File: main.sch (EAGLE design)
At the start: 67 parts, among them IC10 FGPMMOPA6H, IC2 25LC1024-I/P, IC6 MPL3115A2LGA, IC7 FXAS21000, IC8 ADXL343BCCZ, Q1 12MHz, Q2 MCP9700A-E/TO, Q3 FQP7P06, U1 ATMEGA1284P-PU, U2 LT3570EFEPBF, U3 TL431BQLP

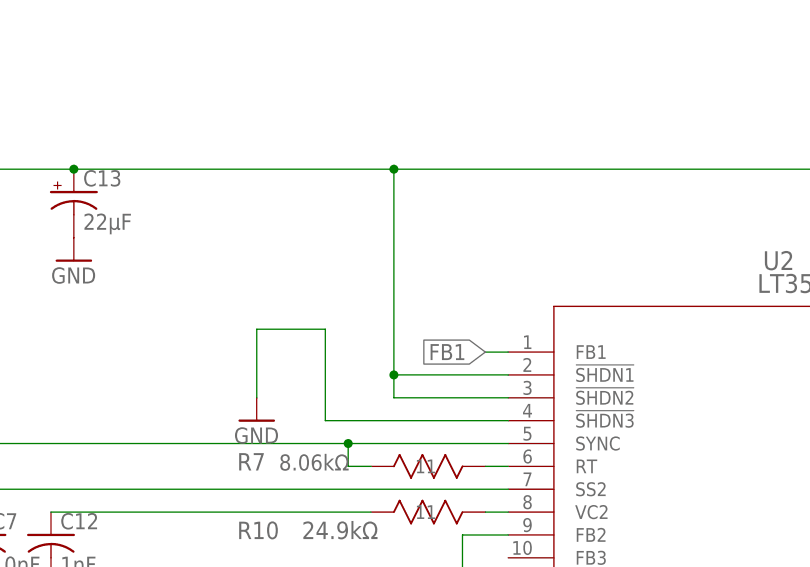
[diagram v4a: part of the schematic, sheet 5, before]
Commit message: Updated Datasheets
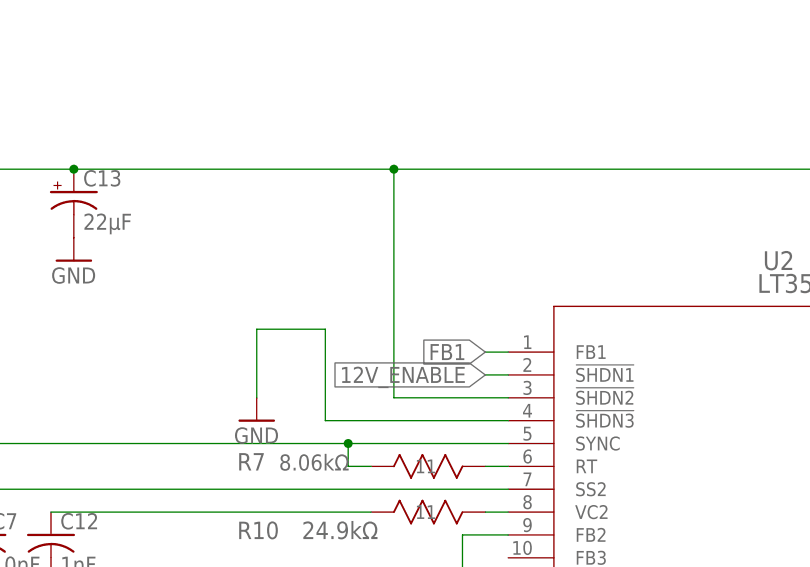
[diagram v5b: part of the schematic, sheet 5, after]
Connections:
- new net 12V_ENABLE: U2.!SHDN1
- net PWR_JUNC: no longer U2.!SHDN1
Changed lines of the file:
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@@
 <grid distance="0.1" unitdist="inch" unit="inch" style="lines" multiple="1" display="no" altdistance="0.01" altunitdist="inch" altunit="inch"/>
 <layers>
-<layer number="1" name="Top" color="4" fill="1" visible="yes" active="no"/>
-<layer number="2" name="Route2" color="1" fill="3" visible="yes" active="no"/>
-<layer number="3" name="Route3" color="4" fill="3" visible="yes" active="no"/>
-<layer number="4" name="Route4" color="1" fill="4" visible="yes" active="no"/>
-<layer number="5" name="Route5" color="4" fill="4" visible="yes" active="no"/>
-<layer number="6" name="Route6" color="1" fill="8" visible="yes" active="no"/>
-<layer number="7" name="Route7" color="4" fill="8" visible="yes" active="no"/>
-<layer number="8" name="Route8" color="1" fill="2" visible="yes" active="no"/>
-<layer number="9" name="Route9" color="4" fill="2" visible="yes" active="no"/>
-<layer number="10" name="Route10" color="1" fill="7" visible="yes" active="no"/>
-<layer number="11" name="Route11" color="4" fill="7" visible="yes" active="no"/>
-<layer number="12" name="Route12" color="1" fill="5" visible="yes" active="no"/>
-<layer number="13" name="Route13" color="4" fill="5" visible="yes" active="no"/>
-<layer number="14" name="Route14" color="1" fill="6" visible="yes" active="no"/>
-<layer number="15" name="Route15" color="4" fill="6" visible="yes" active="no"/>
-<layer number="16" name="Bottom" color="1" fill="1" visible="yes" active="no"/>
-<layer number="17" name="Pads" color="2" fill="1" visible="yes" active="no"/>
-<layer number="18" name="Vias" color="2" fill="1" visible="yes" active="no"/>
-<layer number="19" name="Unrouted" color="6" fill="1" visible="yes" active="no"/>
-<layer number="20" name="Dimension" color="24" fill="1" visible="yes" active="no"/>
-<layer number="21" name="tPlace" color="7" fill="1" visible="yes" active="no"/>
-<layer number="22" name="bPlace" color="7" fill="1" visible="yes" active="no"/>
-<layer number="23" name="tOrigins" color="15" fill="1" visible="yes" active="no"/>
-<layer number="24" name="bOrigins" color="15" fill="1" visible="yes" active="no"/>
-<layer number="25" name="tNames" color="7" fill="1" visible="yes" active="no"/>
-<layer number="26" name="bNames" color="7" fill="1" visible="yes" active="no"/>
-<layer number="27" name="tValues" color="7" fill="1" visible="yes" active="no"/>
-<layer number="28" name="bValues" color="7" fill="1" visible="yes" active="no"/>
+<layer number="1" name="Top" color="4" fill="1" visible="no" active="no"/>
+<layer number="2" name="Route2" color="1" fill="3" visible="no" active="no"/>
+<layer number="3" name="Route3" color="4" fill="3" visible="no" active="no"/>
+<layer number="4" name="Route4" color="1" fill="4" visible="no" active="no"/>
+<layer number="5" name="Route5" color="4" fill="4" visible="no" active="no"/>
+<layer number="6" name="Route6" color="1" fill="8" visible="no" active="no"/>
+<layer number="7" name="Route7" color="4" fill="8" visible="no" active="no"/>
+<layer number="8" name="Route8" color="1" fill="2" visible="no" active="no"/>
+<layer number="9" name="Route9" color="4" fill="2" visible="no" active="no"/>
+<layer number="10" name="Route10" color="1" fill="7" visible="no" active="no"/>
+<layer number="11" name="Route11" color="4" fill="7" visible="no" active="no"/>
+<layer number="12" name="Route12" color="1" fill="5" visible="no" active="no"/>
+<layer number="13" name="Route13" color="4" fill="5" visible="no" active="no"/>
+<layer number="14" name="Route14" color="1" fill="6" visible="no" active="no"/>
+<layer number="15" name="Route15" color="4" fill="6" visible="no" active="no"/>
+<layer number="16" name="Bottom" color="1" fill="1" visible="no" active="no"/>
+<layer number="17" name="Pads" color="2" fill="1" visible="no" active="no"/>
+<layer number="18" name="Vias" color="2" fill="1" visible="no" active="no"/>
+<layer number="19" name="Unrouted" color="6" fill="1" visible="no" active="no"/>
+<layer number="20" name="Dimension" color="24" fill="1" visible="no" active="no"/>
+<layer number="21" name="tPlace" color="7" fill="1" visible="no" active="no"/>
+<layer number="22" name="bPlace" color="7" fill="1" visible="no" active="no"/>
+<layer number="23" name="tOrigins" color="15" fill="1" visible="no" active="no"/>
+<layer number="24" name="bOrigins" color="15" fill="1" visible="no" active="no"/>
+<layer number="25" name="tNames" color="7" fill="1" visible="no" active="no"/>
+<layer number="26" name="bNames" color="7" fill="1" visible="no" active="no"/>
+<layer number="27" name="tValues" color="7" fill="1" visible="no" active="no"/>
+<layer number="28" name="bValues" color="7" fill="1" visible="no" active="no"/>
 <layer number="29" name="tStop" color="7" fill="3" visible="no" active="no"/>
 <layer number="30" name="bStop" color="7" fill="6" visible="no" active="no"/>
@@
 <layer number="35" name="tGlue" color="7" fill="4" visible="no" active="no"/>
 <layer number="36" name="bGlue" color="7" fill="5" visible="no" active="no"/>
-<layer number="37" name="tTest" color="7" fill="1" visible="yes" active="no"/>
-<layer number="38" name="bTest" color="7" fill="1" visible="yes" active="no"/>
+<layer number="37" name="tTest" color="7" fill="1" visible="no" active="no"/>
+<layer number="38" name="bTest" color="7" fill="1" visible="no" active="no"/>
 <layer number="39" name="tKeepout" color="4" fill="11" visible="no" active="no"/>
 <layer number="40" name="bKeepout" color="1" fill="11" visible="no" active="no"/>
@@
 <layer number="44" name="Drills" color="7" fill="1" visible="no" active="no"/>
 <layer number="45" name="Holes" color="7" fill="1" visible="no" active="no"/>
-<layer number="46" name="Milling" color="3" fill="1" visible="yes" active="no"/>
-<layer number="47" name="Measures" color="7" fill="1" visible="yes" active="no"/>
-<layer number="48" name="Document" color="7" fill="1" visible="yes" active="no"/>
-<layer number="49" name="Reference" color="7" fill="1" visible="yes" active="no"/>
-<layer number="50" name="dxf" color="7" fill="1" visible="yes" active="no"/>
-<layer number="51" name="tDocu" color="7" fill="1" visible="yes" active="no"/>
-<layer number="52" name="bDocu" color="7" fill="1" visible="yes" active="no"/>
-<layer number="53" name="tGND_GNDA" color="7" fill="9" visible="yes" active="no"/>
-<layer number="54" name="bGND_GNDA" color="1" fill="9" visible="yes" active="no"/>
-<layer number="56" name="wert" color="7" fill="1" visible="yes" active="no"/>
-<layer number="57" name="tCAD" color="7" fill="1" visible="yes" active="no"/>
-<layer number="59" name="tCarbon" color="7" fill="1" visible="yes" active="no"/>
-<layer number="60" name="bCarbon" color="7" fill="1" visible="yes" active="no"/>
+<layer number="46" name="Milling" color="3" fill="1" visible="no" active="no"/>
+<layer number="47" name="Measures" color="7" fill="1" visible="no" active="no"/>
+<layer number="48" name="Document" color="7" fill="1" visible="no" active="no"/>
+<layer number="49" name="Reference" color="7" fill="1" visible="no" active="no"/>
+<layer number="50" name="dxf" color="7" fill="1" visible="no" active="no"/>
+<layer number="51" name="tDocu" color="7" fill="1" visible="no" active="no"/>
+<layer number="52" name="bDocu" color="7" fill="1" visible="no" active="no"/>
+<layer number="53" name="tGND_GNDA" color="7" fill="9" visible="no" active="no"/>
+<layer number="54" name="bGND_GNDA" color="1" fill="9" visible="no" active="no"/>
+<layer number="56" name="wert" color="7" fill="1" visible="no" active="no"/>
+<layer number="57" name="tCAD" color="7" fill="1" visible="no" active="no"/>
+<layer number="59" name="tCarbon" color="7" fill="1" visible="no" active="no"/>
+<layer number="60" name="bCarbon" color="7" fill="1" visible="no" active="no"/>
 <layer number="88" name="SimResults" color="9" fill="1" visible="yes" active="yes"/>
 <layer number="89" name="SimProbes" color="9" fill="1" visible="yes" active="yes"/>
@@
 <segment>
 <pinref part="U2" gate="A" pin="!SHDN2"/>
-<wire x1="78.74" y1="134.62" x2="78.74" y2="137.16" width="0.1524" layer="91"/>
-<wire x1="78.74" y1="137.16" x2="78.74" y2="160.02" width="0.1524" layer="91"/>
+<wire x1="78.74" y1="134.62" x2="78.74" y2="160.02" width="0.1524" layer="91"/>
 <wire x1="91.44" y1="134.62" x2="78.74" y2="134.62" width="0.1524" layer="91"/>
-<pinref part="U2" gate="A" pin="!SHDN1"/>
-<wire x1="91.44" y1="137.16" x2="78.74" y2="137.16" width="0.1524" layer="91"/>
-<junction x="78.74" y="137.16"/>
 <pinref part="U2" gate="A" pin="VIN1"/>
 <wire x1="157.48" y1="132.08" x2="175.26" y2="132.08" width="0.1524" layer="91"/>
@@
 </segment>
 </net>
+<net name="12V_ENABLE" class="0">
+<segment>
+<pinref part="U2" gate="A" pin="!SHDN1"/>
+<wire x1="91.44" y1="137.16" x2="88.9" y2="137.16" width="0.1524" layer="91"/>
+<label x="88.9" y="137.16" size="1.778" layer="95" rot="R180" xref="yes"/>
+</segment>
+</net>

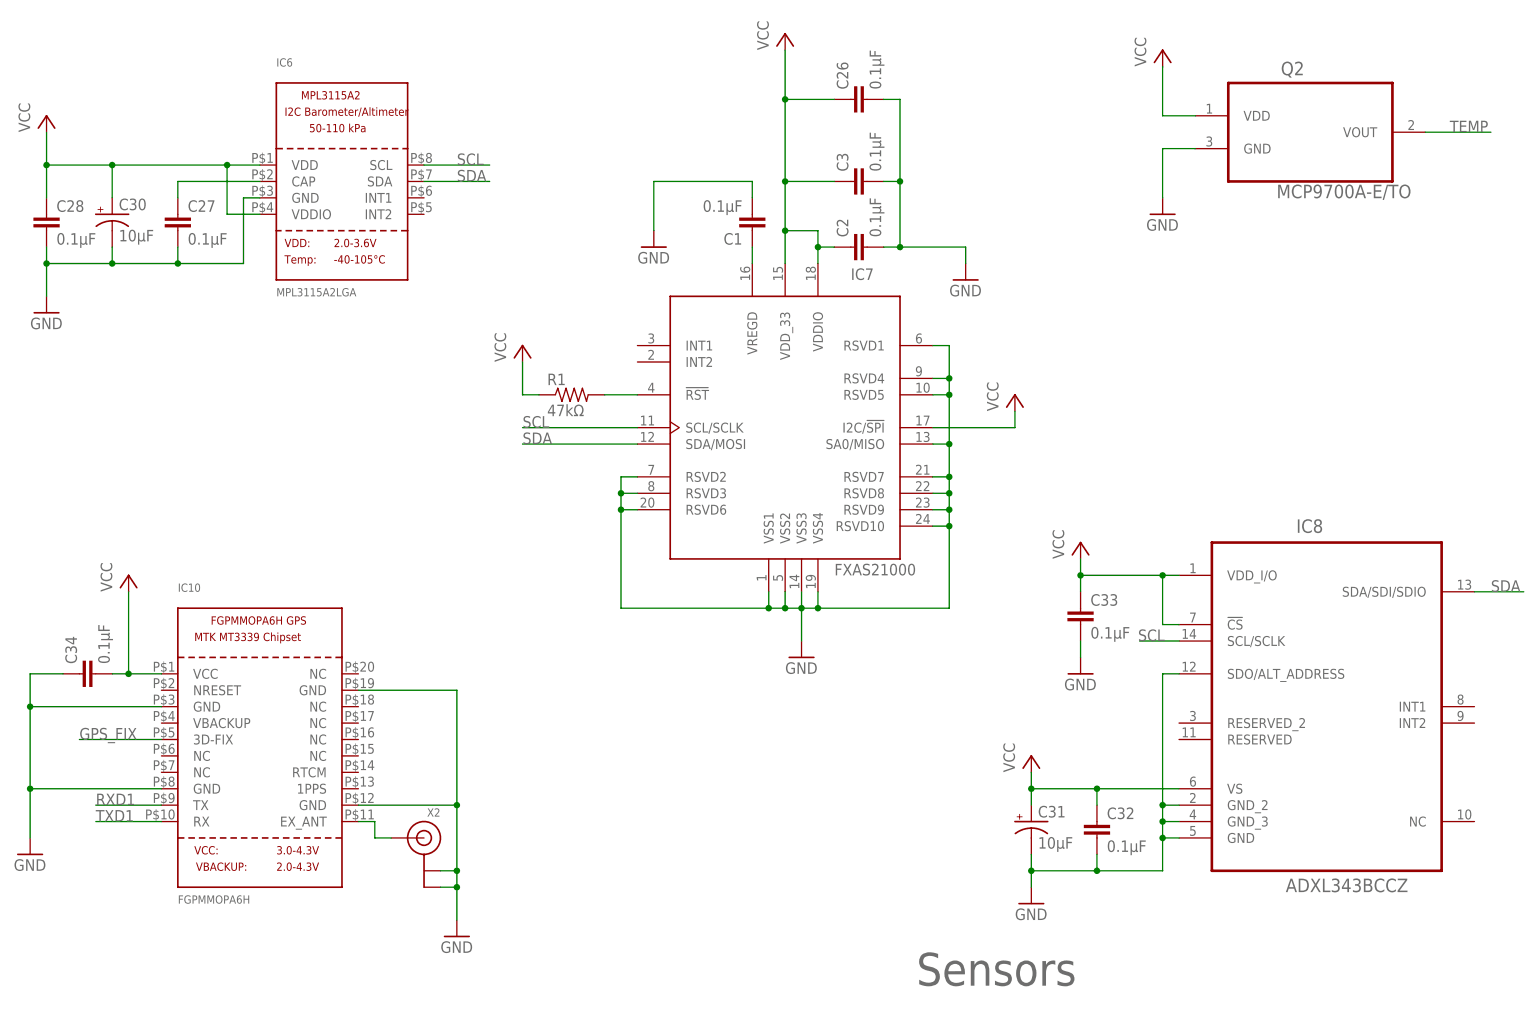
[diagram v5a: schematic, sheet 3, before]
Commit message: Added MCU, Sensors and Radios
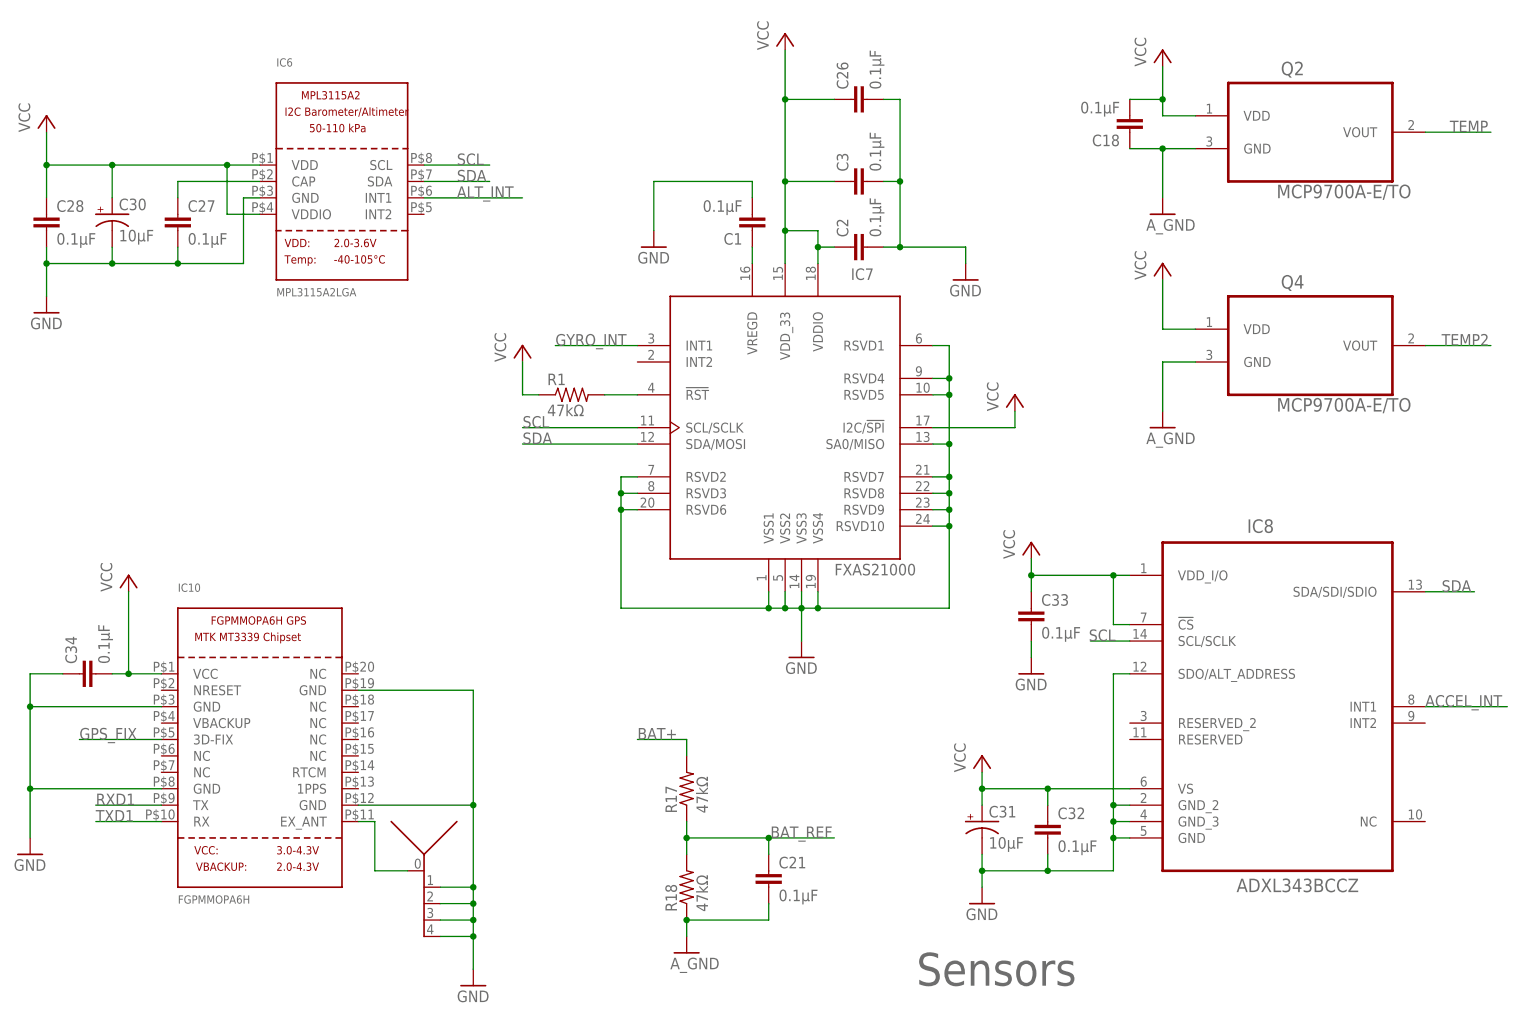
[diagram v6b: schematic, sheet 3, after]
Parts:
- removed X2: (no value), adafruit:ANTENNA_U.FL
- added C18, C21: 0.1µF, rcl:C-EU025-025X050
- added CONSOLE: (no value), pinhead:PINHD-1X4
- added Q4: MCP9700A-E/TO, CU in Space:MCP9700A-E/TO
- added R17, R18: 47kΩ, rcl:R-US_0207/5V
- added R19: 2K2Ω, rcl:R-US_0207/5V
- added X1: 132134RP, CU in Space:132134RP
- DEBUG: device pinhead:PINHD-1X4 -> led:LED5MM
- ICSP: device pinhead:PINHD-2X4 -> pinhead:PINHD-2X3
- Q1: device crystal:CRYSTALHC33U-V -> special:XTAL/S
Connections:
- net U1_RESET renamed RESET
- removed net U2_RESET: ICSP.7
- new net ACCEL_INT: IC8.INT1, U1.PC3
- new net ALT_INT: IC6.INT1, U1.PC2
- new net BAT_REF: C21.1, R17.1, R18.2, U1.PA7
- new net DEBUG_LED: DEBUG.A, U1.PB0
- new net GYRO_INT: IC7.INT1, U1.PC4
- new net N$71: DEBUG.C, R19.1
- new net TEMP2: Q4.VOUT, U1.PA1
- net 12V_ENABLE: now also U1.PC5
- net AVCC: now also C18.2, Q2.VDD, Q4.VDD
- net A_GND: now also C18.1, C21.2, Q2.GND, Q4.GND, R18.1, U1.GND
- net BAT+: now also R17.2
- net GND: now also CONSOLE.4, R19.2, X1.GND@0, X1.GND@1, X1.GND@2, X1.GND@3; no longer DEBUG.4, Q2.GND, U1.GND, X2.GND@0, X2.GND@1
- net N$4: now also X1.ANTENNA; no longer X2.SIGNAL
- net RXD0: now also CONSOLE.2; no longer DEBUG.2
- net TXD0: now also CONSOLE.3; no longer DEBUG.3, ICSP.8
- net VCC: now also CONSOLE.1; no longer DEBUG.1, Q2.VDD
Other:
- moved on the sheet: C31, C32, C33, IC8
